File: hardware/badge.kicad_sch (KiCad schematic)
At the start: 54 parts, among them J1 SAO V.1.69bis master, Q1 BSS138, SW1 power, SW2 SW_Push, SW3 update epaper, U1 Seeed XIAO ESP32-C3, U2 MH-ET_epaper_ 2.13, U3 5V boost converter, U4 TXS0104EPWR

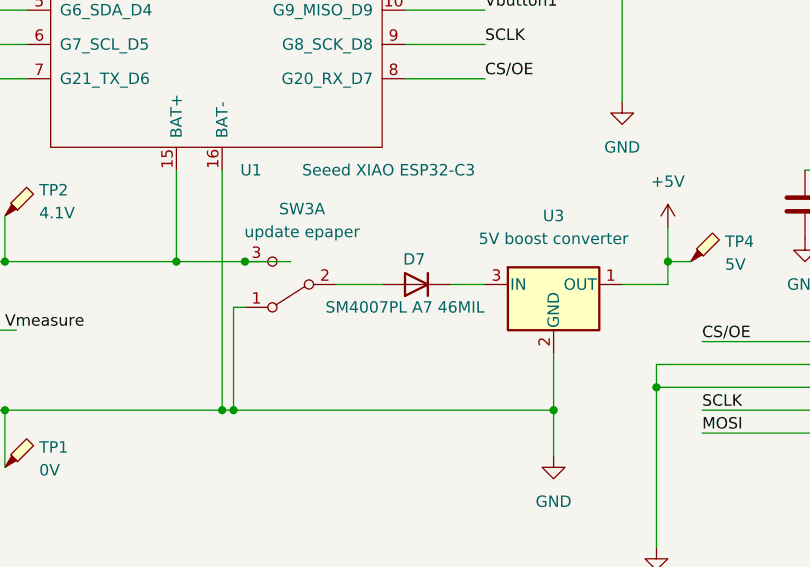
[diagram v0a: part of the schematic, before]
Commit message: remove voltage-drop diode before boost converter
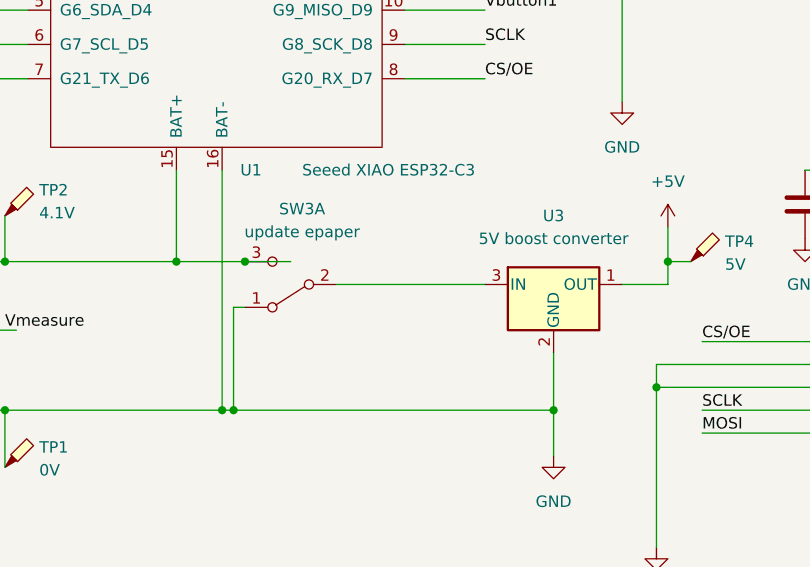
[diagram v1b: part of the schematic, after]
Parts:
- removed D7: SM4007PL A7 46MIL, Diode_SMD:D_SOD-123F, symbol Device:D
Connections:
- net at U3.3 (IN): now also SW3.2 (B)
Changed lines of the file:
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@@
 	(wire
 		(pts
-			(xy 110.49 83.82) (xy 115.57 83.82)
+			(xy 110.49 83.82) (xy 127 83.82)
 		)
 		(stroke
@@
 	(wire
 		(pts
-			(xy 123.19 83.82) (xy 127 83.82)
-		)
-		(stroke
-			(width 0)
-			(type default)
-		)
-	)
-	(wire
-		(pts
 			(xy 238.76 35.56) (xy 238.76 49.53)
 		)
@@
 					(unit 1)
 				)
-			)
-		)
-	)
-	(symbol
-		(lib_id "Device:D")
-		(at 119.38 83.82 180)
-		(unit 1)
-		(exclude_from_sim no)
-		(in_bom yes)
-		(on_board yes)
-		(dnp no)
-		(property "Reference" "D7"
-			(at 119.126 81.026 0)
-			(effects
-				(font
-					(size 1.27 1.27)
-				)
-			)
-		)
-		(property "Value" "SM4007PL A7 46MIL"
-			(at 118.11 86.36 0)
-			(effects
-				(font
-					(size 1.27 1.27)
-				)
-			)
-		)
-		(property "Footprint" "Diode_SMD:D_SOD-123F"
-			(at 119.38 83.82 0)
-			(effects
-				(font
-					(size 1.27 1.27)
-				)
-				(hide yes)
-			)
-		)
-		(property "Datasheet" "https://datasheet.lcsc.com/lcsc/2111101130_YONGYUTAI-SM4007PL-A7-46MIL_C2916249.pdf"
-			(at 119.38 83.82 0)
-			(effects
-				(font
-					(size 1.27 1.27)
-				)
-				(hide yes)
-			)
-		)
-		(property "Description" "Diode"
-			(at 119.38 83.82 0)
-			(effects
-				(font
-					(size 1.27 1.27)
-				)
-				(hide yes)
-			)
-		)
-		(property "Sim.Device" "D"
-			(at 119.38 83.82 0)
-			(effects
-				(font
-					(size 1.27 1.27)
-				)
-				(hide yes)
-			)
-		)
-		(property "Sim.Pins" "1=K 2=A"
-			(at 119.38 83.82 0)
-			(effects
-				(font
-					(size 1.27 1.27)
-				)
-				(hide yes)
-			)
-		)
-		(pin "2"
-		)
-		(pin "1"
-		)
-		(instances
-			(project "badge"
-				(path "/86e9ced6-67f5-4007-880a-280020fc259e"
-					(reference "D7")
-					(unit 1)
-				)

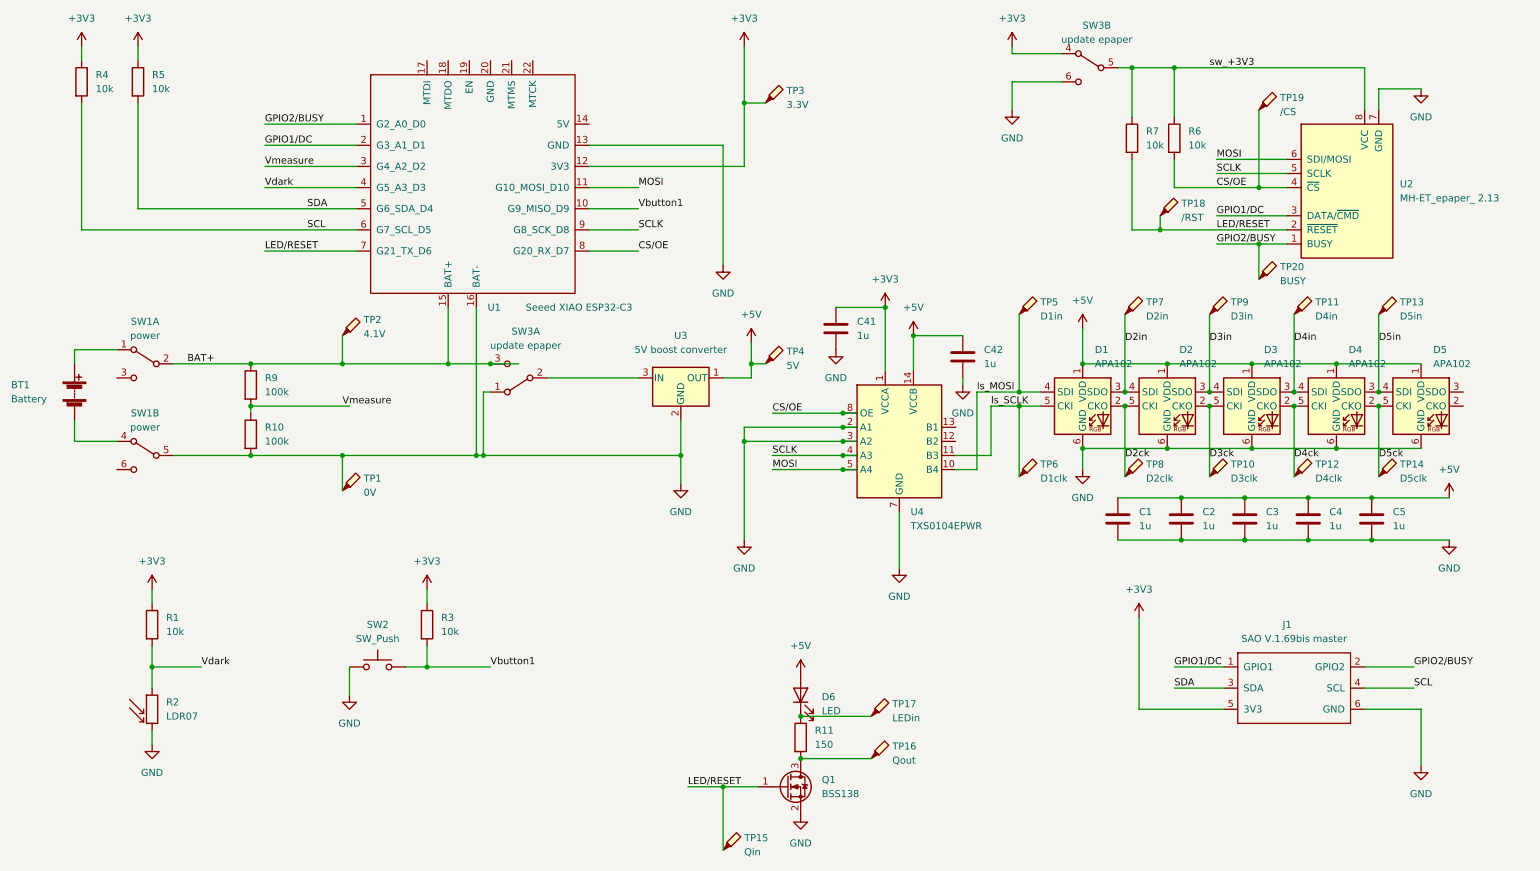
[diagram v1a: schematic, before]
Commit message: cut MOSFET to drive LED with level-shifter; hard-wire /CS and OE
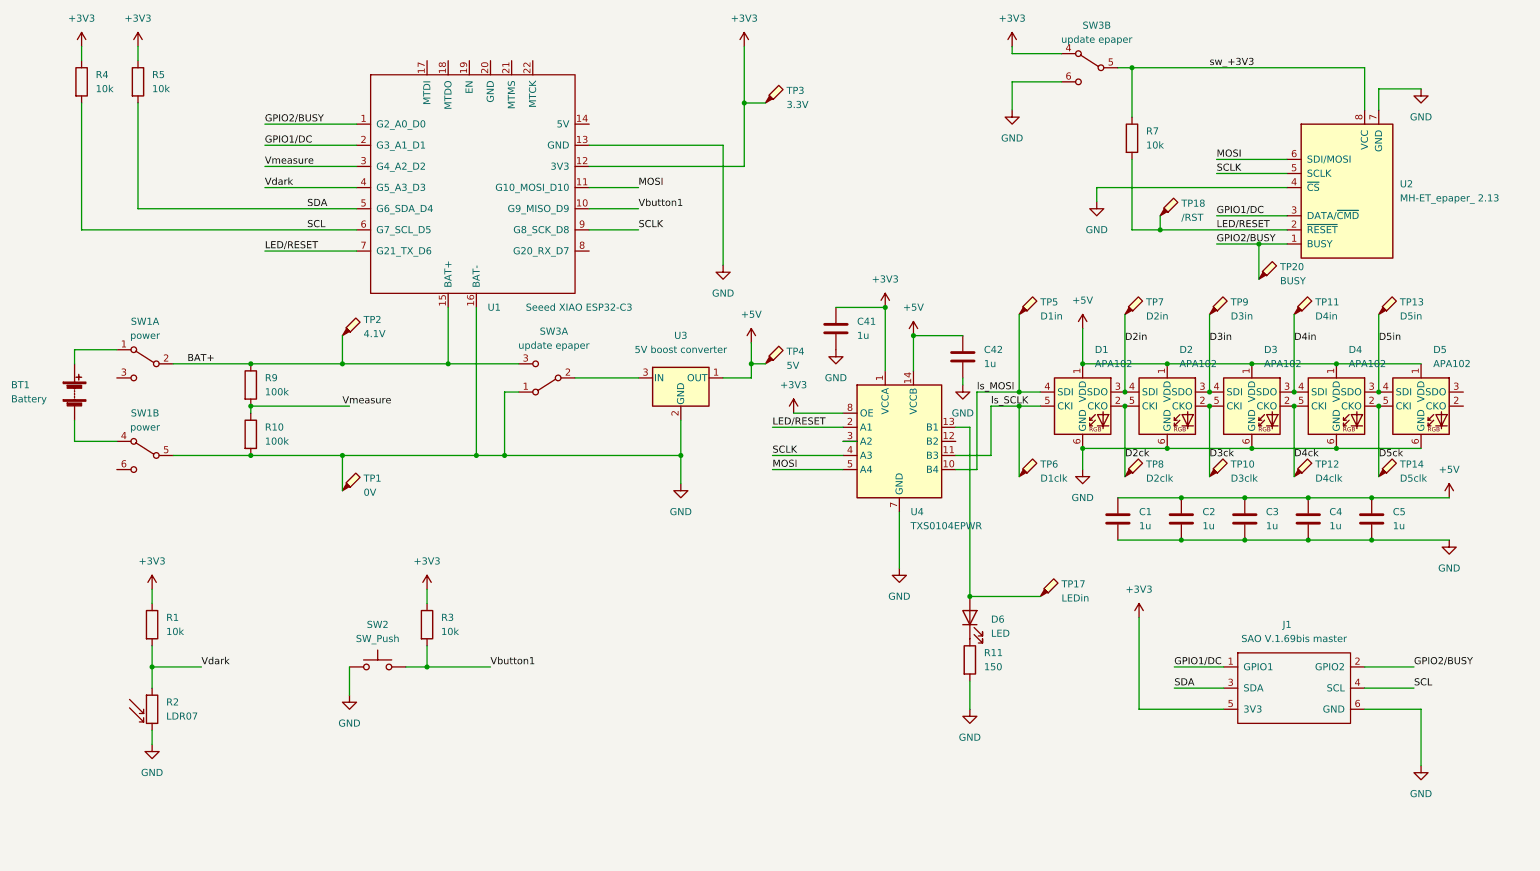
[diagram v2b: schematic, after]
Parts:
- removed Q1: BSS138, Package_TO_SOT_SMD:SOT-23, symbol Device:Q_NMOS_GSD
- removed R6: 10k, Resistor_SMD:R_2010_5025Metric_Pad1.40x2.65mm_HandSolder, symbol Device:R
- removed TP15: Qin, TestPoint:TestPoint_Pad_1.5x1.5mm, symbol Connector:TestPoint_Probe
- removed TP16: Qout, TestPoint:TestPoint_Pad_1.5x1.5mm, symbol Connector:TestPoint_Probe
- removed TP19: /CS, TestPoint:TestPoint_Pad_1.5x1.5mm, symbol Connector:TestPoint_Probe
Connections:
- net +3V3: now also U4.8 (OE)
- net +5V: no longer D6.2 (A)
- net GND: now also R11.2, U2.4 (~{CS}); no longer U4.2 (A1), U4.3 (A2)
- net LED/RESET: now also U4.2 (A1)
- net at D6.1 (K), R11.1: no longer TP17.1
- net at U4.13 (B1): now also D6.2 (A), TP17.1
- removed net CS/OE: U1.8 (G20_RX_D7), U2.4 (~{CS}), U4.8 (OE)
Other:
- moved on the sheet: D6, R11, SW3A, TP17

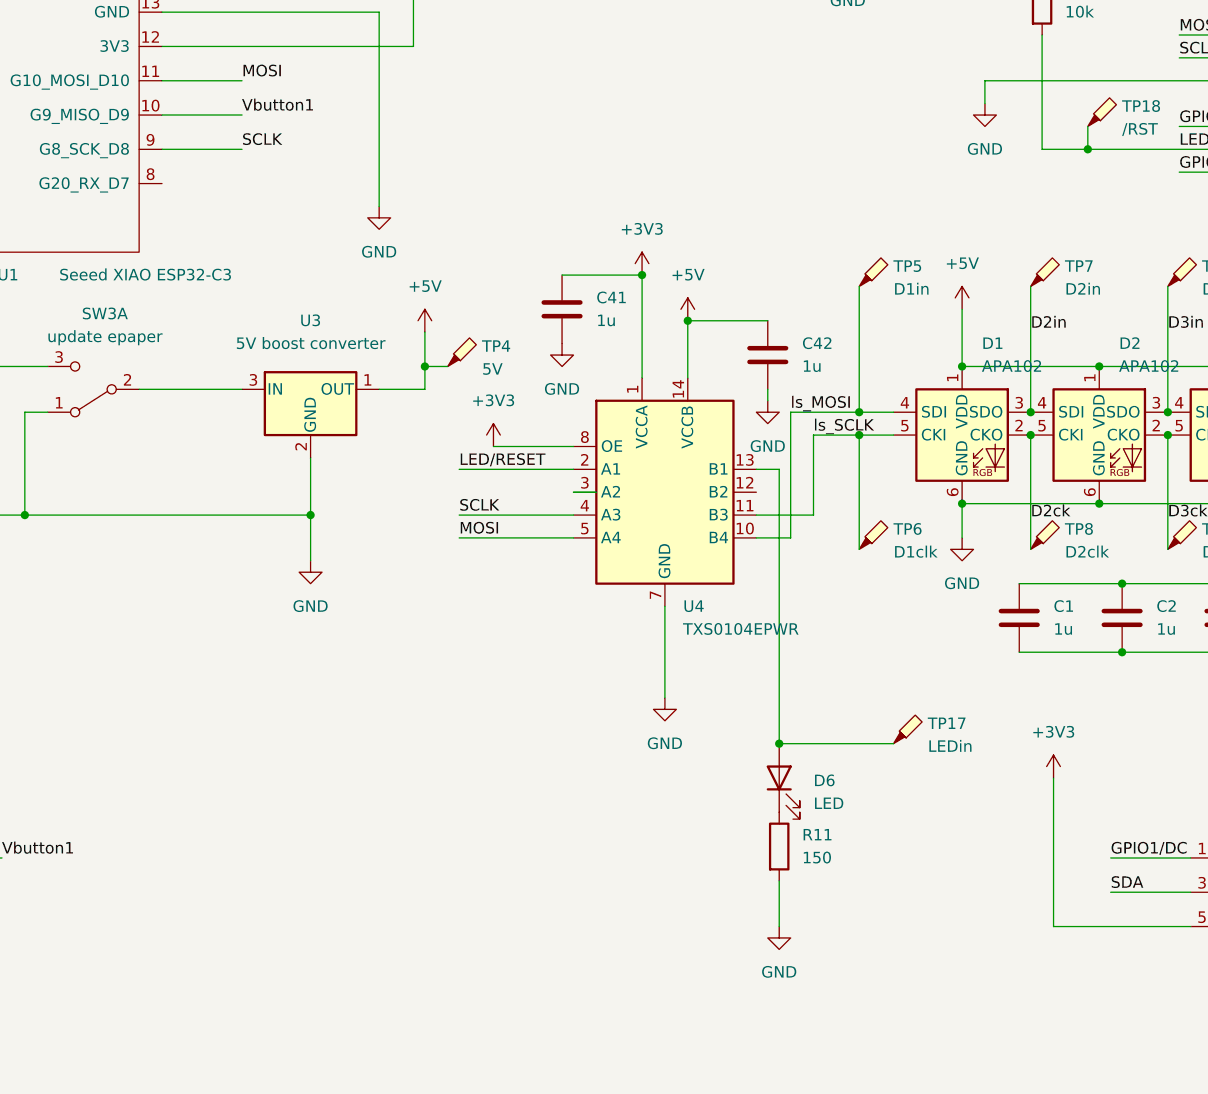
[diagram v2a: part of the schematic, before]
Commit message: level-shifter datasheet dire warnings re OE wrt power-good means OE is back
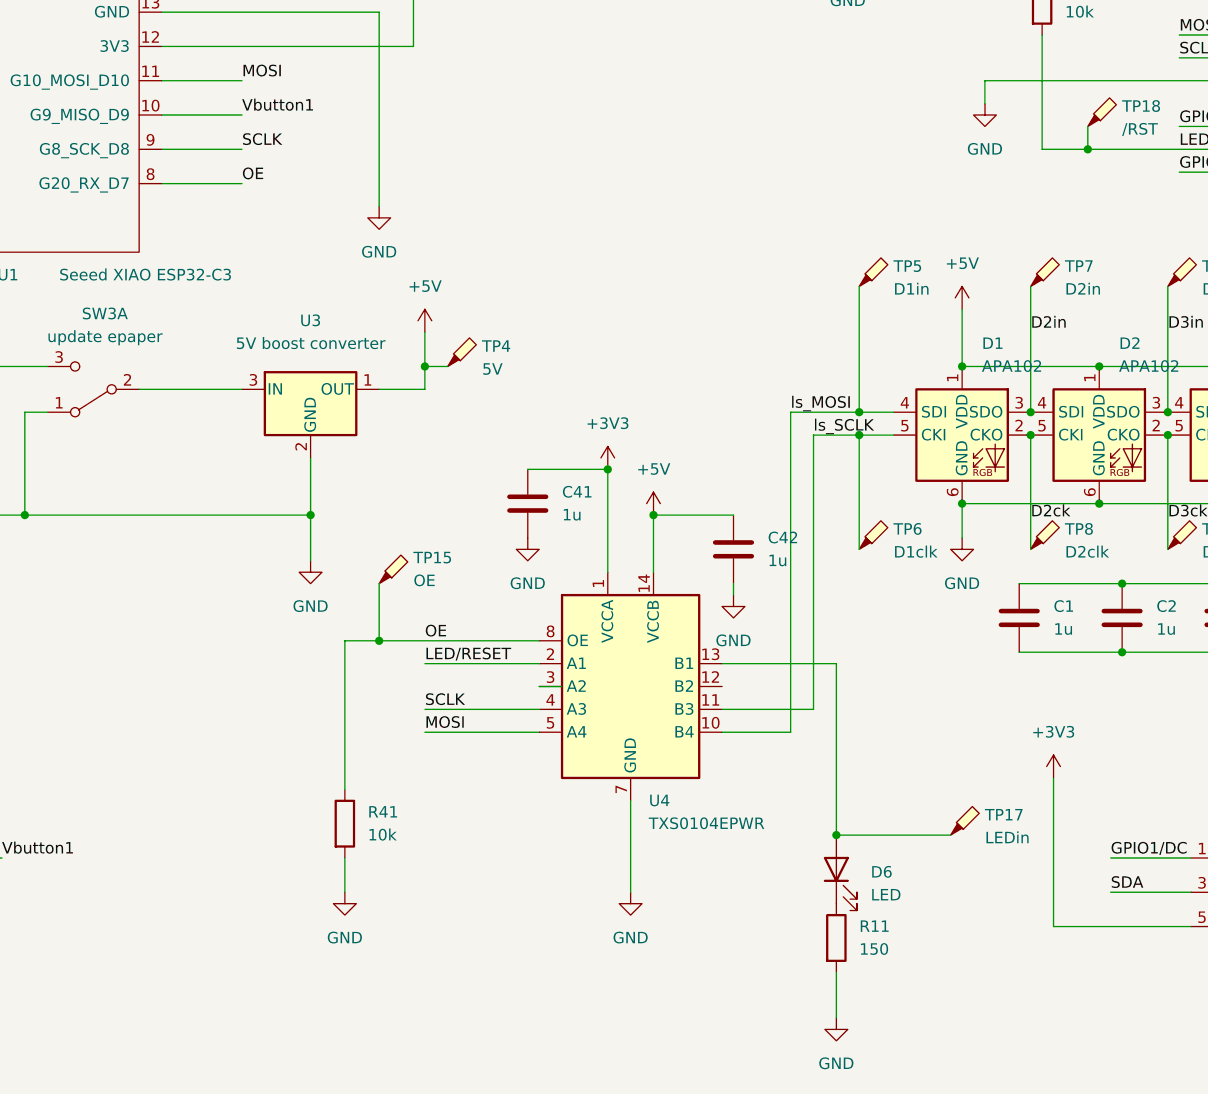
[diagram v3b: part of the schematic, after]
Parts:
- added R41: 10k, Resistor_SMD:R_2010_5025Metric_Pad1.40x2.65mm_HandSolder, symbol Device:R
- added TP15: OE, TestPoint:TestPoint_Pad_1.5x1.5mm, symbol Connector:TestPoint_Probe
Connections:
- net +3V3: no longer U4.8 (OE)
- net GND: now also R41.2
- net OE: now reaches U1.8 (G20_RX_D7)
- net OE: now also U4.8 (OE), R41.1, TP15.1
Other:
- moved on the sheet: C41, C42, D6, R11, TP17, U4

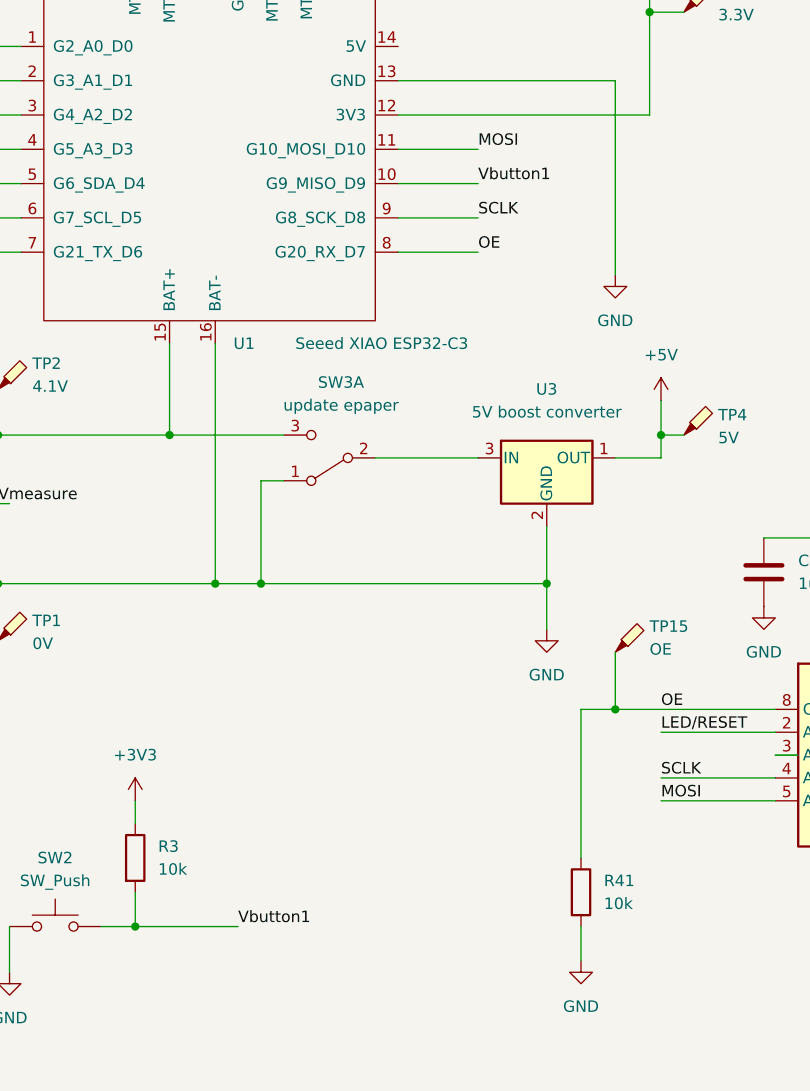
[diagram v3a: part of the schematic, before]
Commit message: improved DRC results and some track routing
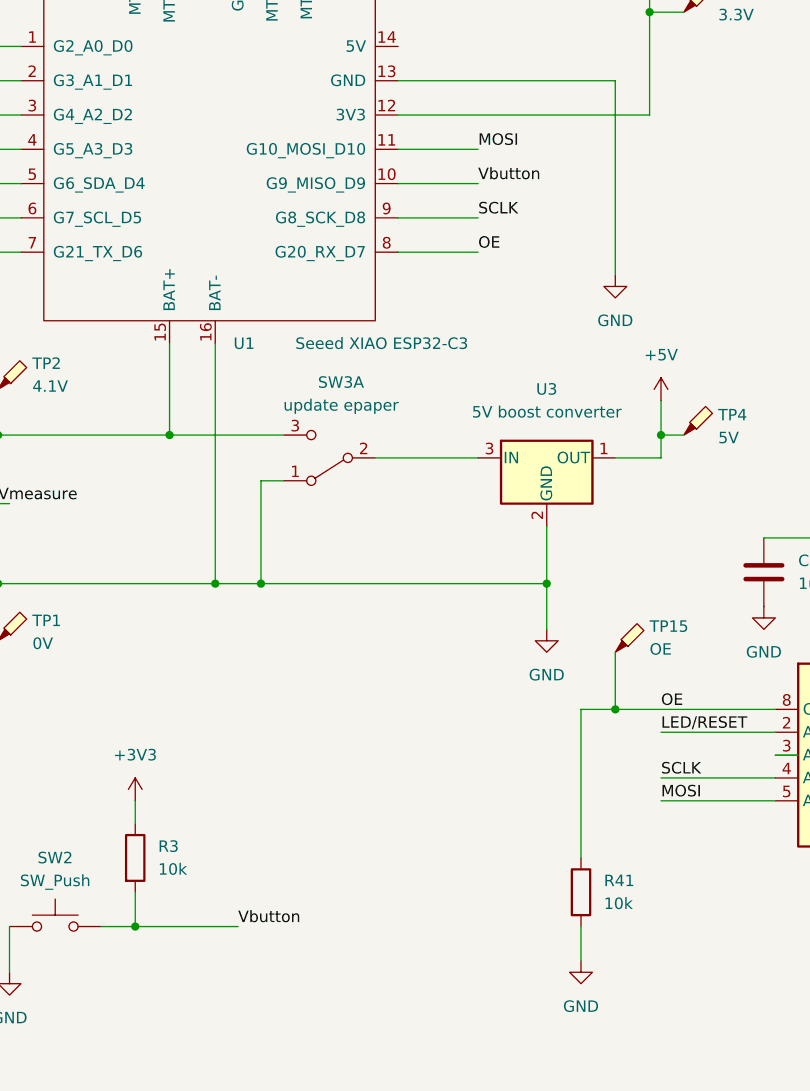
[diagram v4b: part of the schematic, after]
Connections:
- net Vbutton1 renamed Vbutton
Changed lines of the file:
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@@
 		)
 	)
-	(label "Vbutton1"
+	(label "Vbutton"
 		(at 100.33 135.89 0)
 		(fields_autoplaced yes)
@@
 		)
 	)
-	(label "Vbutton1"
+	(label "Vbutton"
 		(at 127 53.34 0)
 		(fields_autoplaced yes)

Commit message: restore CS control; swap TH-LED to back
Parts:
- J1: value SAO V.1.69bis master -> SAO V.1.69bis host
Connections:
- net GND: no longer U2.4 (~{CS})
- net OE renamed OE/cs
- net OE/cs: now also U2.4 (~{CS})
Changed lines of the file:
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@@
 	(wire
 		(pts
-			(xy 209.55 52.07) (xy 209.55 49.53)
+			(xy 147.32 77.47) (xy 147.32 81.28)
 		)
 		(stroke
@@
 	(wire
 		(pts
-			(xy 147.32 77.47) (xy 147.32 81.28)
+			(xy 195.58 72.39) (xy 195.58 86.36)
 		)
 		(stroke
@@
 	(wire
 		(pts
-			(xy 195.58 72.39) (xy 195.58 86.36)
+			(xy 92.71 71.12) (xy 92.71 81.28)
 		)
 		(stroke
@@
 	(wire
 		(pts
-			(xy 92.71 71.12) (xy 92.71 81.28)
+			(xy 215.9 27.94) (xy 215.9 36.83)
 		)
 		(stroke
@@
 	(wire
 		(pts
-			(xy 215.9 27.94) (xy 215.9 36.83)
+			(xy 231.14 49.53) (xy 243.84 49.53)
 		)
 		(stroke
@@
 	(wire
 		(pts
-			(xy 209.55 49.53) (xy 243.84 49.53)
-		)
-		(stroke
-			(width 0)
-			(type default)
-		)
-	)
-	(wire
-		(pts
 			(xy 223.52 139.7) (xy 232.41 139.7)
 		)
@@
 		)
 	)
-	(label "OE"
+	(label "OE{slash}cs"
 		(at 127 60.96 0)
 		(fields_autoplaced yes)
@@
 		)
 	)
-	(label "OE"
+	(label "OE{slash}cs"
 		(at 147.32 111.76 0)
 		(fields_autoplaced yes)
@@
 		)
 	)
+	(label "OE{slash}cs"
+		(at 231.14 49.53 0)
+		(fields_autoplaced yes)
+		(effects
+			(font
+				(size 1.27 1.27)
+			)
+			(justify left bottom)
+		)
+	)
 	(label "GPIO1{slash}DC"
 		(at 59.69 41.91 0)
@@
 			)
 		)
-		(property "Value" "SAO V.1.69bis master"
+		(property "Value" "SAO V.1.69bis host"
 			(at 245.11 130.81 0)
 			(effects
@@
 					(unit 1)
 				)
-			)
-		)
-	)
-	(symbol
-		(lib_id "power:GND")
-		(at 209.55 52.07 0)
-		(unit 1)
-		(exclude_from_sim no)
-		(in_bom yes)
-		(on_board yes)
-		(dnp no)
-		(fields_autoplaced yes)
-		(property "Reference" "#PWR01"
-			(at 209.55 58.42 0)
-			(effects
-				(font
-					(size 1.27 1.27)
-				)
-				(hide yes)
-			)
-		)
-		(property "Value" "GND"
-			(at 209.55 57.15 0)
-			(effects
-				(font
-					(size 1.27 1.27)
-				)
-			)
-		)
-		(property "Footprint" ""
-			(at 209.55 52.07 0)
-			(effects
-				(font
-					(size 1.27 1.27)
-				)
-				(hide yes)
-			)
-		)
-		(property "Datasheet" ""
-			(at 209.55 52.07 0)
-			(effects
-				(font
-					(size 1.27 1.27)
-				)
-				(hide yes)
-			)
-		)
-		(property "Description" ""
-			(at 209.55 52.07 0)
-			(effects
-				(font
-					(size 1.27 1.27)
-				)
-				(hide yes)
-			)
-		)
-		(pin "1"
-		)
-		(instances
-			(project "badge"
-				(path "/86e9ced6-67f5-4007-880a-280020fc259e"
-					(reference "#PWR01")
-					(unit 1)
-				)
